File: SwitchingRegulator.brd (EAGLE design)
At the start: 111.3 x 67.1 mm, 35 parts, among them J1 APP_2POS_CONFIG5V_HORIZ, J2 APP_2POS_CONFIG5V_HORIZ, J4 APP_2POS_CONFIG12V_HORIZ, Q2 Q_CSD18532KCSPCB, Q3 Q_CSD18532KCSPCB, U1 OKI-78SR-5/1.5-W36HC

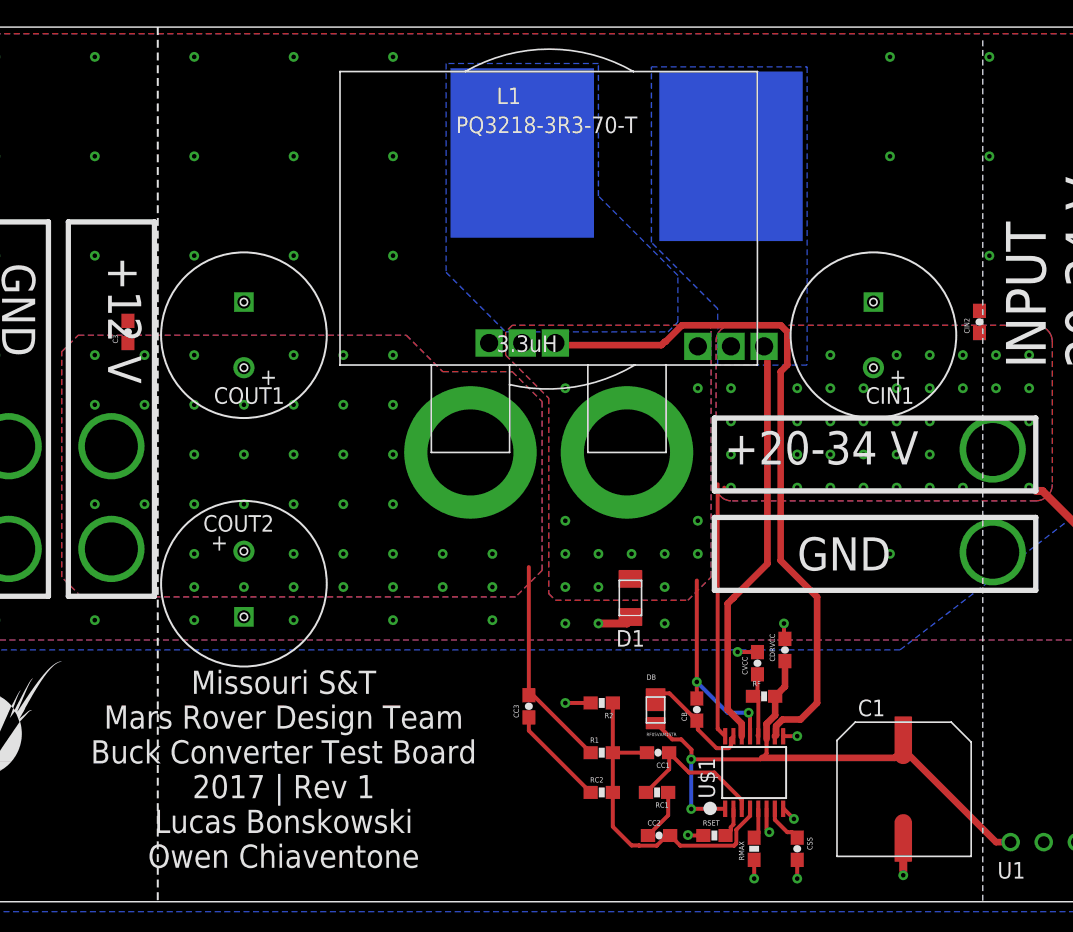
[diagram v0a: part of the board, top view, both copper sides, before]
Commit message: Switched to upright mosfets, adjusted board accordingly
Spread out some of the signal components on the bottom side of the board.  Adjusted power planes to compensate for new mosfet orientation.
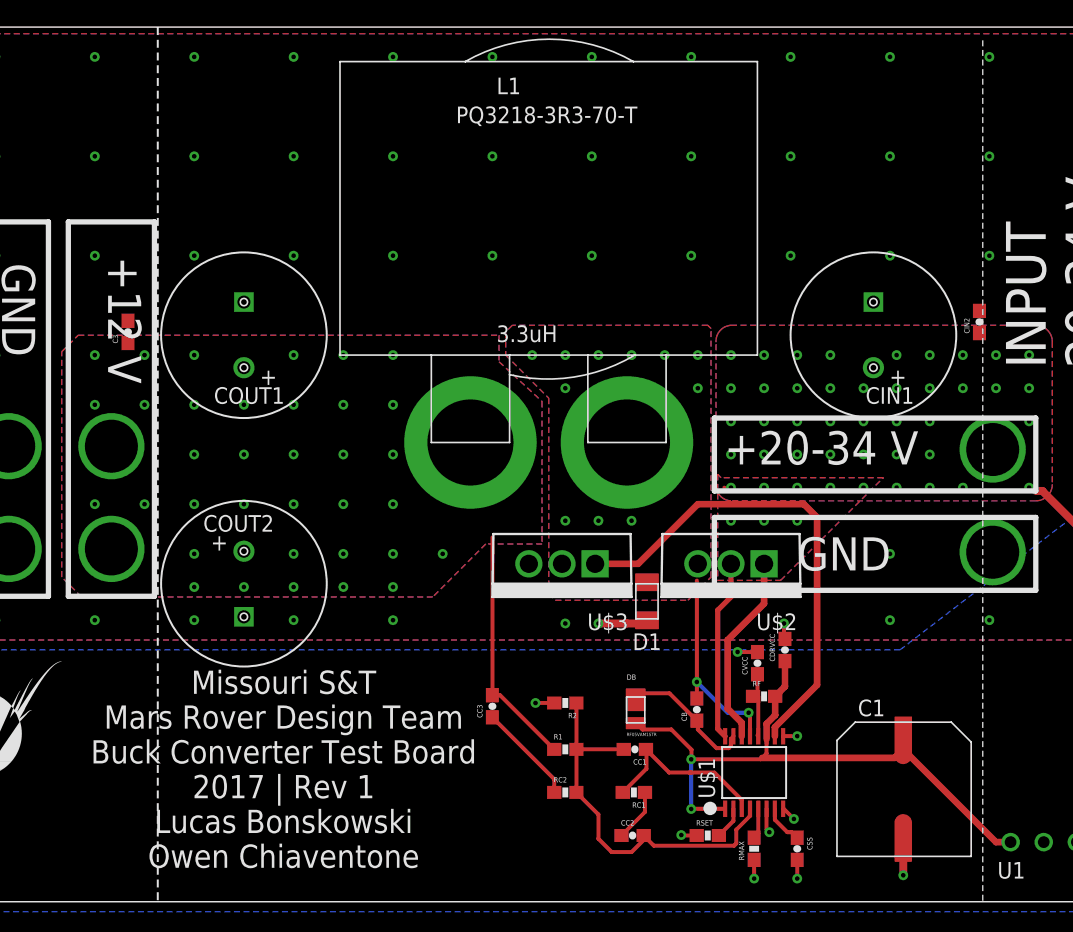
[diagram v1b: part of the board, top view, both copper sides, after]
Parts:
- removed Q2, Q3: Q_CSD18532KCSPCB, MRDT-2014-All:TO-220-FLAT
- added U$2, U$3: IPP052N06L3GXKSA1, buckconverter:TO-220
- RMAX: value 30k -> 16.5k
- RSET: value 10k -> 19.1k
- moved R1 2.81 mm to (61.0, 11.7)
- moved CC3 2.79 mm to (55.4, 15.0)
- moved R2 2.79 mm to (61.0, 15.2)
- moved RC2 2.79 mm to (61.0, 8.38)
- moved CC2 2.03 mm to (66.1, 5.08)
- moved CC1 1.80 mm to (66.3, 11.7)
- moved RC1 1.78 mm to (66.2, 8.38)
- moved DB 1.52 mm to (65.7, 13.7)
- moved D1 1.30 mm to (68.1, 24.4)
- moved L1 0.76 mm to (43.7, 41.9)
- moved RSET 0.51 mm to (71.9, 5.08)
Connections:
- net GND: now also U$3.3; no longer Q3.3
- net N$16: now also U$3.1; no longer Q3.1
- net N$17: now also U$2.3, U$3.2; no longer Q2.3, Q3.2, Q3.4
- net N$2: now also U$2.1; no longer Q2.1
- net VBATT: now also U$2.2; no longer Q2.2, Q2.4
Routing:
- net N$2: track 31.9 -> 14.8 mm
- net N$16: track 53.2 -> 37.5 mm
- net VBATT: track 48.2 -> 42.5 mm, vias 36 -> 46
- net N$11: track 26.0 -> 30.0 mm
- net N$7: track 11.5 -> 13.9 mm
- net VOUT12+: track 16.4 -> 18.6 mm, vias 38 -> 35
- net N$1: track 8.75 -> 10.3 mm
- net 5V: track 48.5 -> 49.6 mm
- net GND: track 18.1 -> 18.8 mm, vias 64 -> 77
- net N$17: vias 14 -> 13

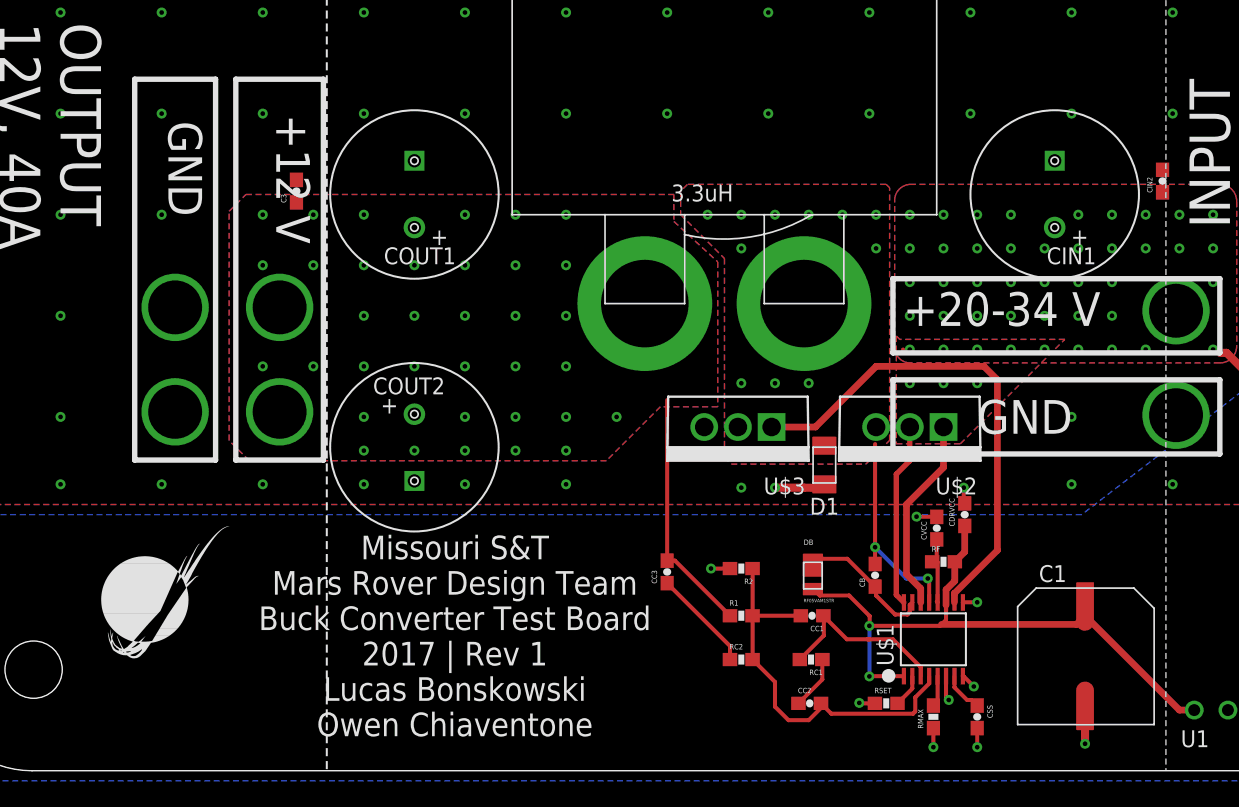
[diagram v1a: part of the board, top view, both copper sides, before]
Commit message: Improved silkscreen labeling
Moved labeling to tplace layer because tsilk layer does not pront in manufacturing. Elarged labels on each resistor and capacitor to help in populating the board.
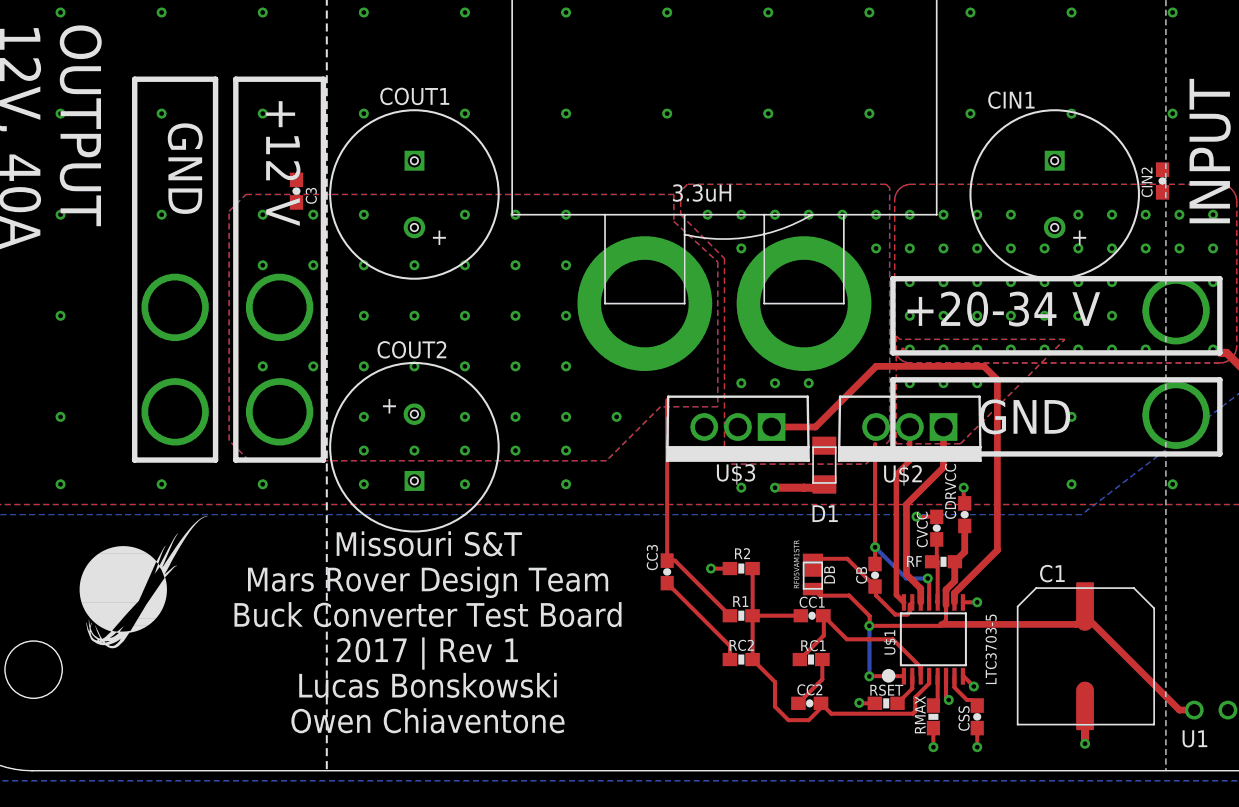
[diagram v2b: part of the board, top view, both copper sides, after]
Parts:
- moved LOGO1 1.80 mm to (11.1, 8.38)

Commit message: Heatsinks added, rearranges needed
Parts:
- added U$4, U$5: 530002B02500G, buckconverter:RADIAL_FIN_HEATSINK
- moved D1 143.1 mm to (210.1, 42.4)
- moved LOGO1 38.1 mm to (-14.6, 36.6)
- moved C3 37.4 mm to (38.4, 79.5)
- moved COUT1 36.3 mm to (30.2, 79.2)
- moved H3 36.1 mm to (111.4, 96.8)
- moved CIN2 36.1 mm to (97.5, 80.3)
- moved CIN1 35.8 mm to (85.1, 79.2)
- moved L1 35.8 mm to (44.2, 77.7)
- moved H4 35.8 mm to (8.13, 96.8)
- moved J1 34.5 mm to (-9.40, 65.5)
- moved J2 34.5 mm to (-9.40, 57.7)
- moved U$2 30.5 mm to (73.9, 56.4)
- moved COUT2 12.3 mm to (30.2, 35.1)
- moved U$3 11.4 mm to (61.2, 37.3)
- moved CDRVCC 11.0 mm to (67.6, 23.6)
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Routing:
- net VBATT: track 42.5 -> 0.09 mm, vias 46 -> 38
- net N$16: track 37.5 -> 0.00 mm
- net N$2: track 14.8 -> 0.00 mm
- net VOUT12+: track 18.6 -> 6.46 mm, vias 35 -> 30
- net N$17: track 15.8 -> 8.07 mm
- net GND: track 18.8 -> 16.9 mm, vias 77 -> 75
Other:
- board size 111.3 x 67.1 mm -> 115.6 x 102.1 mm

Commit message: Power traces turned horizontal
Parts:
- moved LOGO1 158.2 mm to (136.3, -10.9)
- moved D1 123.8 mm to (86.9, 54.6), turned to 0 degrees
- moved CIN2 68.6 mm to (56.6, 25.1), turned to 270 degrees
- moved CIN1 65.3 mm to (48.5, 25.1), turned to 0 degrees
- moved COUT1 54.3 mm to (35.1, 25.1), turned to 0 degrees
- moved C3 41.6 mm to (22.4, 41.1), turned to 180 degrees
- moved U$3 37.8 mm to (94.7, 54.9), turned to 90 degrees
- moved U$4 36.6 mm to (91.2, 54.9), turned to 90 degrees
- moved J2 32.8 mm to (-9.91, 24.9)
- moved J1 32.8 mm to (-9.91, 32.8)
- moved L1 30.4 mm to (26.7, 52.8)
- moved H3 25.9 mm to (111.1, 70.9)
- moved H4 25.9 mm to (7.87, 70.9)
- moved U$2 18.3 mm to (75.4, 38.1), turned to 90 degrees
- moved COUT2 16.1 mm to (21.3, 48.5), turned to 270 degrees
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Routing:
- net N$16: track 0.00 -> 60.9 mm
- net N$2: track 0.00 -> 39.7 mm
- net VBATT: track 0.09 -> 30.1 mm, vias 38 -> 3
- net 5V: track 49.6 -> 73.8 mm
- net N$17: track 8.07 -> 32.1 mm, vias 13 -> 2
- net VOUT12+: track 6.46 -> 18.0 mm, vias 30 -> 4
- net GND: track 16.9 -> 14.7 mm, vias 75 -> 69
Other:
- board size 115.6 x 102.1 mm -> 115.6 x 77.5 mm

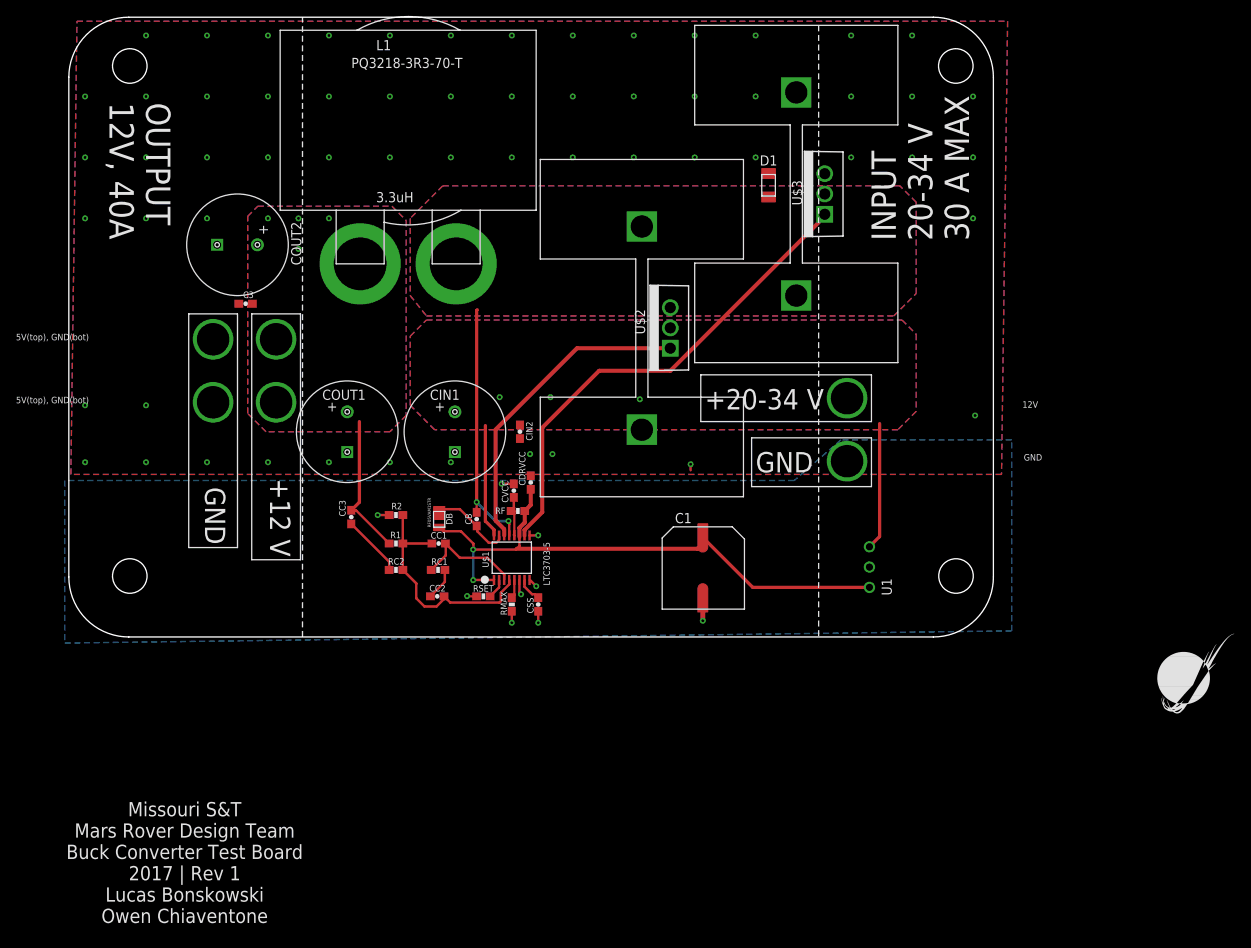
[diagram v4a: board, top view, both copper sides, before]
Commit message: Final revision for testing
Finished via stitching
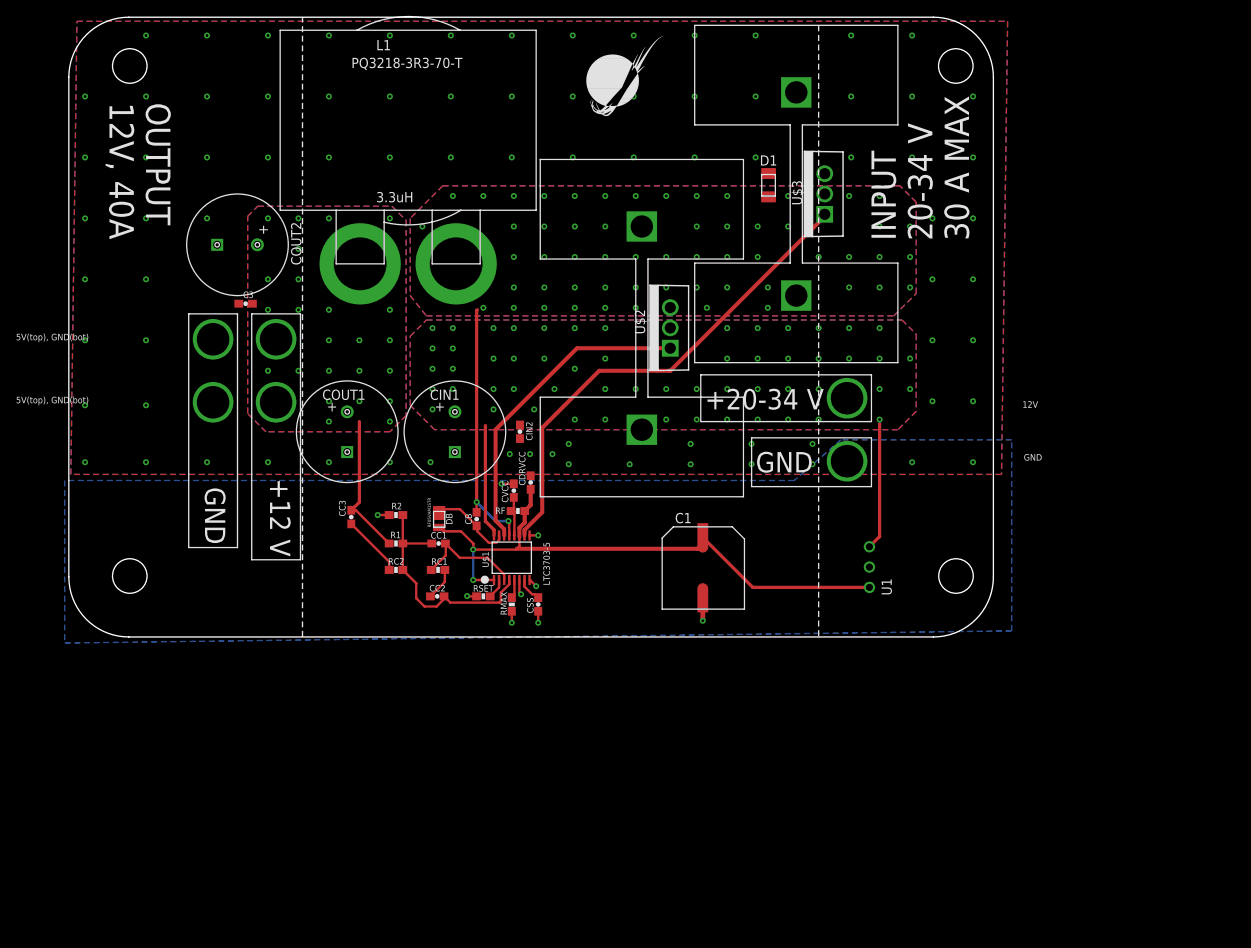
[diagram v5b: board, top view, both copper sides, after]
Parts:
- moved LOGO1 103.3 mm to (64.9, 63.8)
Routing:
- net GND: track 14.7 -> 13.9 mm, vias 69 -> 90
- net VOUT12+: vias 4 -> 24
- net VBATT: vias 3 -> 56
- net N$17: vias 2 -> 59
